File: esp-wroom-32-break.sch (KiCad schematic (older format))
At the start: 17 parts, among them CON1 Micro_SD_Card, IC1 FT232RQ, P1 CONN_01X18, P2 CONN_01X18, P3 USB_OTG, P4 Switch, U1 ESP32-WROOM, U2 NJU7223DL1-33

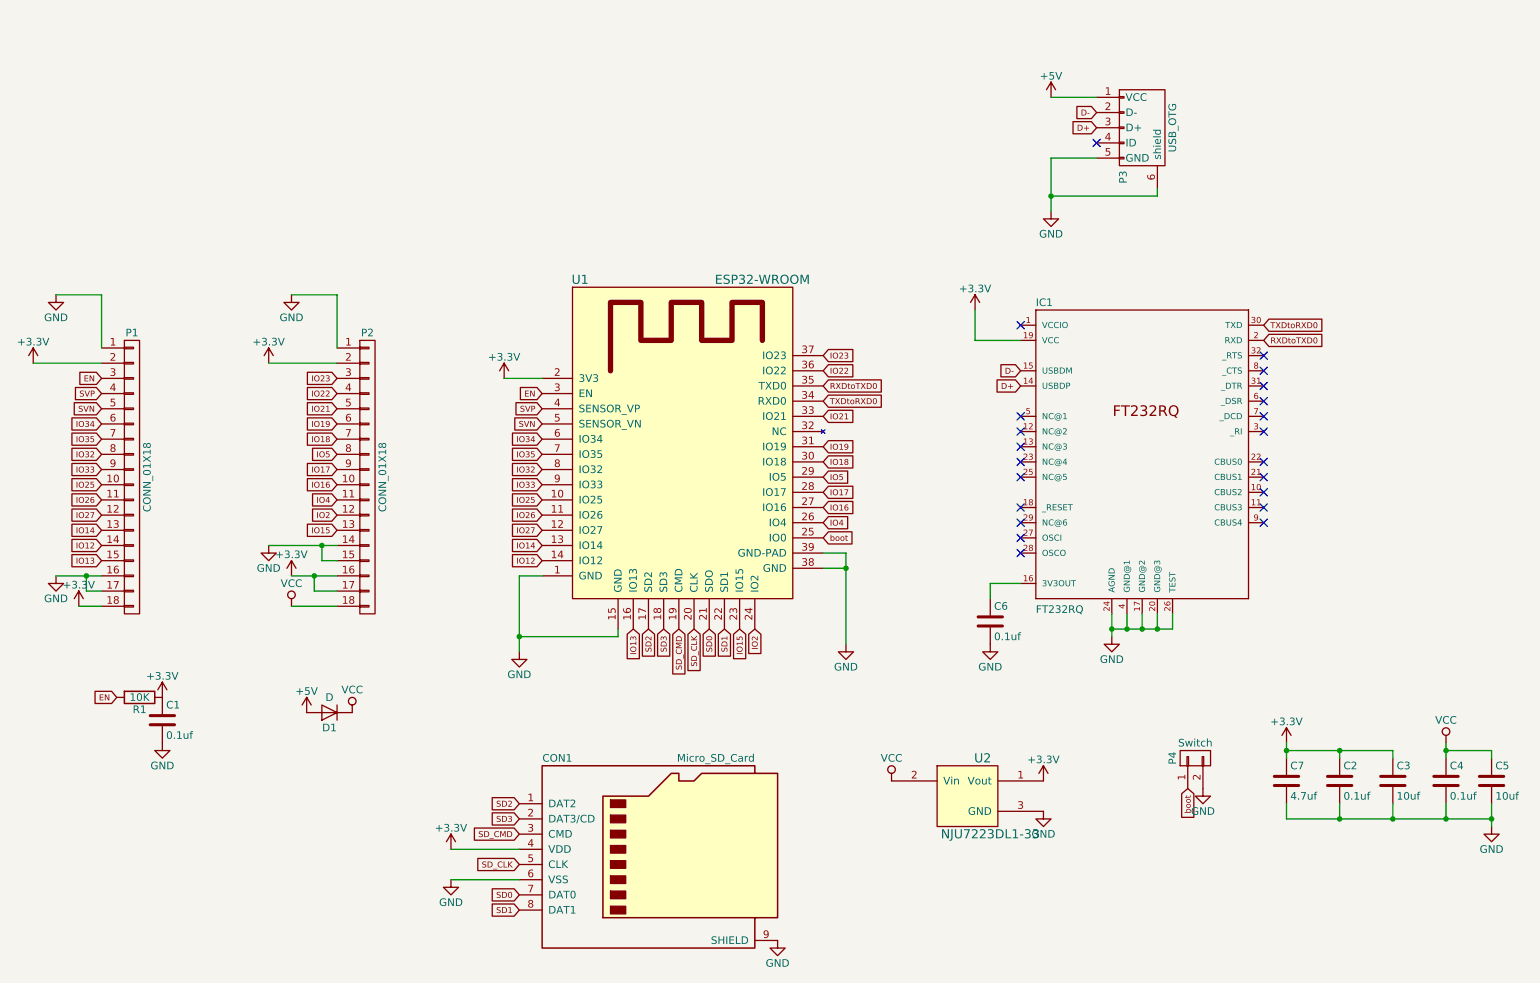
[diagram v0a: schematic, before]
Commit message: Change to 17 pins socket and remove redundant condensors
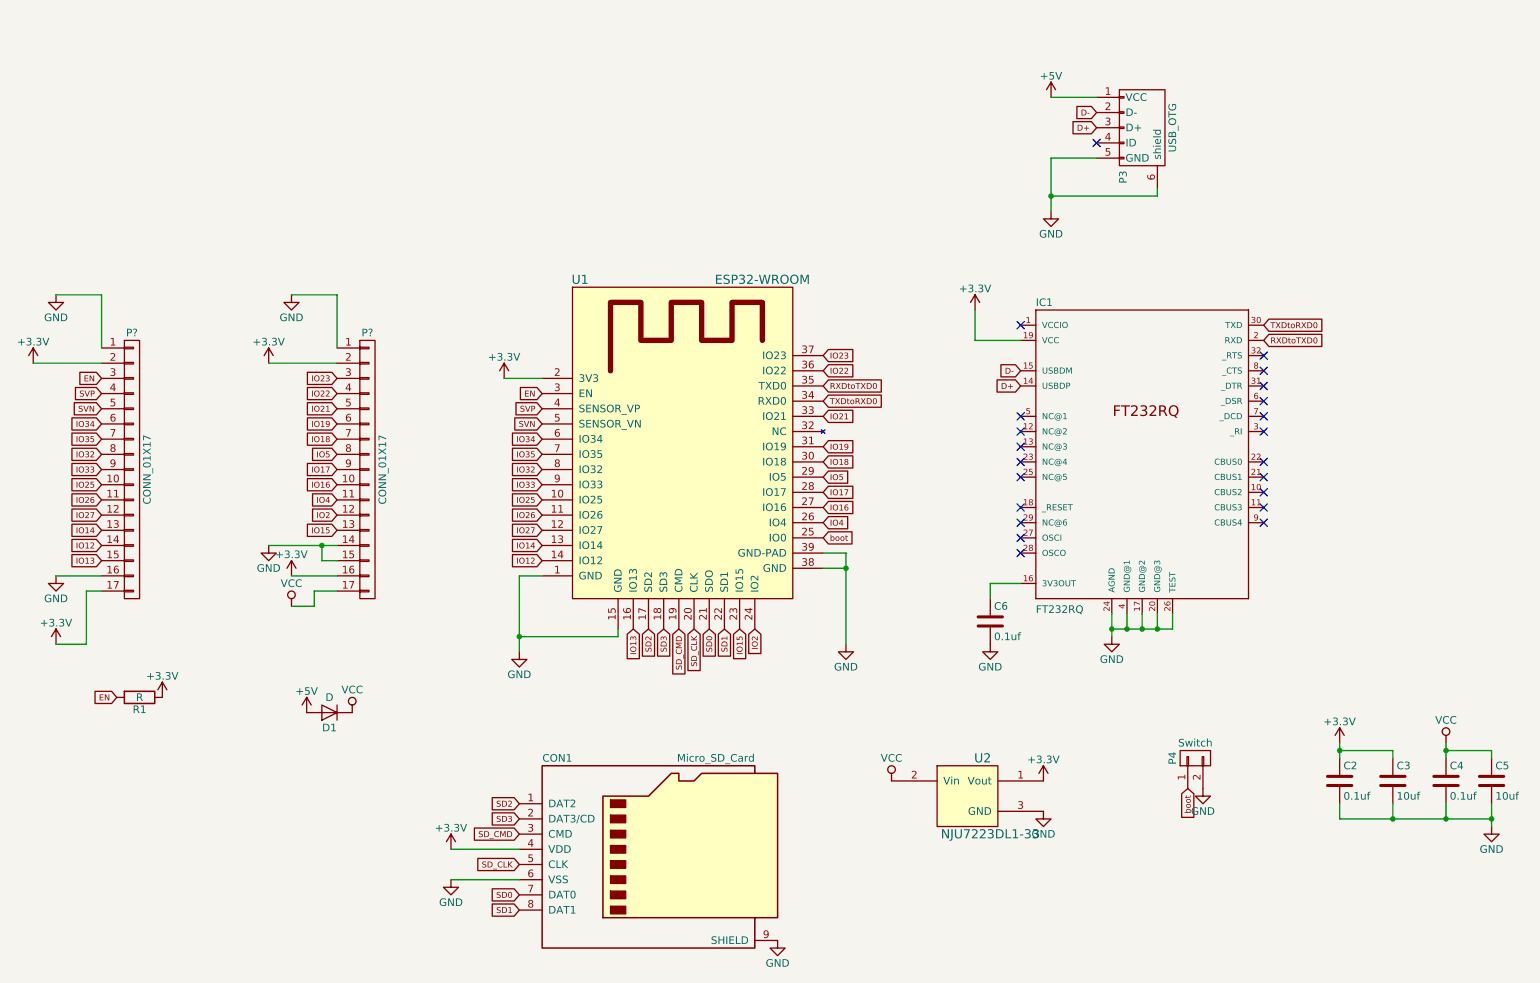
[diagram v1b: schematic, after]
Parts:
- removed C1: 0.1uf, Capacitors_SMD:C_0603, symbol C
- removed C7: 4.7uf, Capacitors_SMD:C_0603, symbol C
- removed P1, P2: CONN_01X18, Pin_Headers:Pin_Header_Straight_1x18_Pitch2.54mm, symbol CONN_01X18
- added P? (x2): CONN_01X17, symbol CONN_01X17
- R1: value 10K -> R
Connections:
- net +3V3: now also P?.16 (P16), P?.17 (P17), P?.2 (P2), P?.2 (P2)
- net EN: now also P?.3 (P3)
- net GND: now also P?.1 (P1), P?.1 (P1), P?.14 (P14), P?.15 (P15), P?.16 (P16)
- net IO12: now also P?.14 (P14)
- net IO13: now also P?.15 (P15)
- net IO14: now also P?.13 (P13)
- net IO15: now also P?.13 (P13)
- net IO16: now also P?.10 (P10)
- net IO17: now also P?.9 (P9)
- net IO18: now also P?.7 (P7)
- net IO19: now also P?.6 (P6)
- net IO2: now also P?.12 (P12)
- net IO21: now also P?.5 (P5)
- net IO22: now also P?.4 (P4)
- net IO23: now also P?.3 (P3)
- net IO25: now also P?.10 (P10)
- net IO26: now also P?.11 (P11)
- net IO27: now also P?.12 (P12)
- net IO32: now also P?.8 (P8)
- net IO33: now also P?.9 (P9)
- net IO34: now also P?.6 (P6)
- net IO35: now also P?.7 (P7)
- net IO4: now also P?.11 (P11)
- net IO5: now also P?.8 (P8)
- net SVN: now also P?.5 (P5)
- net SVP: now also P?.4 (P4)
- net VCC: now also P?.17 (P17)
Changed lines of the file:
@@
 IO15
-$Comp
-L CONN_01X18 P1
-U 1 1 5894820C
-P 1850 3800
-F 0 "P1" H 1850 4750 50  0000 C CNN
-F 1 "CONN_01X18" V 1950 3800 50  0000 C CNN
-F 2 "Pin_Headers:Pin_Header_Straight_1x18_Pitch2.54mm" H 1850 3800 50  0001 C CNN
-F 3 "" H 1850 3800 50  0000 C CNN
-	1    1850 3800
-	1    0    0    -1
-$EndComp
-$Comp
-L CONN_01X18 P2
-U 1 1 5894825B
-P 3400 3800
-F 0 "P2" H 3400 4750 50  0000 C CNN
-F 1 "CONN_01X18" V 3500 3800 50  0000 C CNN
-F 2 "Pin_Headers:Pin_Header_Straight_1x18_Pitch2.54mm" H 3400 3800 50  0001 C CNN
-F 3 "" H 3400 3800 50  0000 C CNN
-	1    3400 3800
-	1    0    0    -1
-$EndComp
 $Comp
 L +3.3V #PWR011
@@
 L +3.3V #PWR017
 U 1 1 58948E57
-P 1500 4650
-F 0 "#PWR017" H 1500 4500 50  0001 C CNN
-F 1 "+3.3V" H 1500 4790 50  0000 C CNN
-F 2 "" H 1500 4650 50  0000 C CNN
-F 3 "" H 1500 4650 50  0000 C CNN
-	1    1500 4650
+P 1350 4900
+F 0 "#PWR017" H 1350 4750 50  0001 C CNN
+F 1 "+3.3V" H 1350 5040 50  0000 C CNN
+F 2 "" H 1350 4900 50  0000 C CNN
+F 3 "" H 1350 4900 50  0000 C CNN
+	1    1350 4900
 	1    0    0    -1
 $EndComp
@@
 P 1900 5250
 F 0 "R1" V 1980 5250 50  0000 C CNN
-F 1 "10K" V 1900 5250 50  0000 C CNN
+F 1 "R" V 1900 5250 50  0000 C CNN
 F 2 "Resistors_SMD:R_0603" V 1830 5250 50  0001 C CNN
 F 3 "" H 1900 5250 50  0000 C CNN
@@
 F 3 "" H 2050 5250 50  0000 C CNN
 	1    2050 5250
-	1    0    0    -1
-$EndComp
-$Comp
-L C C1
-U 1 1 589493A7
-P 2050 5400
-F 0 "C1" H 2075 5500 50  0000 L CNN
-F 1 "0.1uf" H 2075 5300 50  0000 L CNN
-F 2 "Capacitors_SMD:C_0603" H 2088 5250 50  0001 C CNN
-F 3 "" H 2050 5400 50  0000 C CNN
-	1    2050 5400
-	1    0    0    -1
-$EndComp
-$Comp
-L GND #PWR021
-U 1 1 589493DB
-P 2050 5550
-F 0 "#PWR021" H 2050 5300 50  0001 C CNN
-F 1 "GND" H 2050 5400 50  0000 C CNN
-F 2 "" H 2050 5550 50  0000 C CNN
-F 3 "" H 2050 5550 50  0000 C CNN
-	1    2050 5550
 	1    0    0    -1
 $EndComp
@@
 L +3.3V #PWR026
 U 1 1 5894AD31
-P 9450 5550
-F 0 "#PWR026" H 9450 5400 50  0001 C CNN
-F 1 "+3.3V" H 9450 5690 50  0000 C CNN
-F 2 "" H 9450 5550 50  0000 C CNN
-F 3 "" H 9450 5550 50  0000 C CNN
-	1    9450 5550
+P 9800 5550
+F 0 "#PWR026" H 9800 5400 50  0001 C CNN
+F 1 "+3.3V" H 9800 5690 50  0000 C CNN
+F 2 "" H 9800 5550 50  0000 C CNN
+F 3 "" H 9800 5550 50  0000 C CNN
+	1    9800 5550
 	1    0    0    -1
 $EndComp
@@
 	1    0    0    -1
 $EndComp
-Wire Wire Line
-	4300 3150 4550 3150
-Wire Wire Line
-	6400 4300 6550 4300
-Wire Wire Line
-	6550 4300 6550 4900
-Wire Wire Line
-	6400 4400 6550 4400
-Connection ~ 6550 4400
-Wire Wire Line
-	4550 4450 4400 4450
-Wire Wire Line
-	4400 4450 4400 4950
-Wire Wire Line
-	5050 4800 5050 4850
-Wire Wire Line
-	5050 4850 4400 4850
-Connection ~ 4400 4850
-Wire Wire Line
-	7900 1300 8200 1300
-Wire Wire Line
-	7900 1700 8200 1700
-Wire Wire Line
-	3950 6250 4400 6250
-Wire Wire Line
-	3950 6450 4400 6450
-Wire Wire Line
-	1650 3050 1200 3050
-Wire Wire Line
-	1350 2600 1650 2600
-Wire Wire Line
-	1650 2600 1650 2950
-Wire Wire Line
-	3200 3050 2750 3050
-Wire Wire Line
-	2900 2600 3200 2600
-Wire Wire Line
-	3200 2600 3200 2950
-Wire Wire Line
-	2900 4650 3200 4650
-Wire Wire Line
-	2900 4450 3200 4450
-Wire Wire Line
-	3050 4450 3050 4550
-Wire Wire Line
-	3050 4550 3200 4550
-Connection ~ 3050 4450
-Wire Wire Line
-	1500 4650 1650 4650
-Wire Wire Line
-	1350 4450 1650 4450
-Wire Wire Line
-	1550 4450 1550 4550
-Wire Wire Line
-	1550 4550 1650 4550
-Connection ~ 1550 4450
-Wire Wire Line
-	2750 4250 3200 4250
-Wire Wire Line
-	3100 4250 3100 4350
-Wire Wire Line
-	3100 4350 3200 4350
-Connection ~ 3100 4250
-Wire Wire Line
-	7400 2900 7700 2900
-Wire Wire Line
-	8300 4700 8300 4850
-Wire Wire Line
-	8300 4800 8700 4800
-Wire Wire Line
-	8700 4800 8700 4700
-Connection ~ 8300 4800
-Wire Wire Line
-	8400 4700 8400 4800
-Connection ~ 8400 4800
-Wire Wire Line
-	8500 4700 8500 4800
-Connection ~ 8500 4800
-Wire Wire Line
-	8600 4700 8600 4800
-Connection ~ 8600 4800
-Wire Wire Line
-	7400 2700 7400 2900
-Wire Wire Line
-	10150 5600 10150 5650
-Wire Wire Line
-	10500 5550 10500 5650
-Wire Wire Line
-	10500 5600 10800 5600
-Wire Wire Line
-	10800 5600 10800 5650
-Connection ~ 10500 5600
-Wire Wire Line
-	9800 5950 9800 6050
-Wire Wire Line
-	9450 6050 10800 6050
-Wire Wire Line
-	10800 5950 10800 6100
-Connection ~ 10800 6050
-Wire Wire Line
-	10500 5950 10500 6050
-Connection ~ 10500 6050
-Wire Wire Line
-	10150 5950 10150 6050
-Connection ~ 10150 6050
 $Comp
 L NJU7223DL1-33 U2
@@
 $EndComp
 NoConn ~ 7700 2800
-Wire Wire Line
-	7900 1700 7900 2050
-Wire Wire Line
-	8600 1900 8600 1950
-Wire Wire Line
-	8600 1950 7900 1950
-Connection ~ 7900 1950
 $Comp
 L FT232RQ IC1
@@
 	1    0    0    -1
 $EndComp
+$Comp
+L CONN_01X17 P?
+U 1 1 58A7A438
+P 1850 3750
+F 0 "P?" H 1850 4650 50  0000 C CNN
+F 1 "CONN_01X17" V 1950 3750 50  0000 C CNN
+F 2 "" H 1850 3750 50  0000 C CNN
+F 3 "" H 1850 3750 50  0000 C CNN
+	1    1850 3750
+	1    0    0    -1
+$EndComp
+$Comp
+L CONN_01X17 P?
+U 1 1 58A7A491
+P 3400 3750
+F 0 "P?" H 3400 4650 50  0000 C CNN
+F 1 "CONN_01X17" V 3500 3750 50  0000 C CNN
+F 2 "" H 3400 3750 50  0000 C CNN
+F 3 "" H 3400 3750 50  0000 C CNN
+	1    3400 3750
+	1    0    0    -1
+$EndComp
+Wire Wire Line
+	4300 3150 4550 3150
+Wire Wire Line
+	6400 4300 6550 4300
+Wire Wire Line
+	6550 4300 6550 4900
+Wire Wire Line
+	6400 4400 6550 4400
+Connection ~ 6550 4400
+Wire Wire Line
+	4550 4450 4400 4450
+Wire Wire Line
+	4400 4450 4400 4950
+Wire Wire Line
+	5050 4800 5050 4850
+Wire Wire Line
+	5050 4850 4400 4850
+Connection ~ 4400 4850
+Wire Wire Line
+	7900 1300 8200 1300
+Wire Wire Line
+	7900 1700 8200 1700
+Wire Wire Line
+	3950 6250 4400 6250
+Wire Wire Line
+	3950 6450 4400 6450
+Wire Wire Line
+	1650 3050 1200 3050
+Wire Wire Line
+	1350 2600 1650 2600
+Wire Wire Line
+	1650 2600 1650 2950
+Wire Wire Line
+	3200 3050 2750 3050
+Wire Wire Line
+	2900 2600 3200 2600
+Wire Wire Line
+	3200 2600 3200 2950
+Wire Wire Line
+	2900 4450 3200 4450
+Wire Wire Line
+	1350 4450 1650 4450
+Wire Wire Line
+	2750 4250 3200 4250
+Wire Wire Line
+	3100 4250 3100 4350
+Wire Wire Line
+	3100 4350 3200 4350
+Connection ~ 3100 4250
+Wire Wire Line
+	7400 2900 7700 2900
+Wire Wire Line
+	8300 4700 8300 4850
+Wire Wire Line
+	8300 4800 8700 4800
+Wire Wire Line
+	8700 4800 8700 4700
+Connection ~ 8300 4800
+Wire Wire Line
+	8400 4700 8400 4800
+Connection ~ 8400 4800
+Wire Wire Line
+	8500 4700 8500 4800
+Connection ~ 8500 4800
+Wire Wire Line
+	8600 4700 8600 4800
+Connection ~ 8600 4800
+Wire Wire Line
+	7400 2700 7400 2900
+Wire Wire Line
+	10150 5600 10150 5650
+Wire Wire Line
+	10500 5550 10500 5650
+Wire Wire Line
+	10500 5600 10800 5600
+Wire Wire Line
+	10800 5600 10800 5650
+Connection ~ 10500 5600
+Wire Wire Line
+	10800 5950 10800 6100
+Connection ~ 10800 6050
+Wire Wire Line
+	10500 5950 10500 6050
+Connection ~ 10500 6050
+Wire Wire Line
+	10150 5950 10150 6050
+Connection ~ 10150 6050
+Wire Wire Line
+	7900 1700 7900 2050
+Wire Wire Line
+	8600 1900 8600 1950
+Wire Wire Line
+	8600 1950 7900 1950
+Connection ~ 7900 1950
 Wire Wire Line
 	7500 4600 7500 4500
 Wire Wire Line
 	7500 4500 7700 4500
-$Comp
-L C C7
-U 1 1 58987CEA
-P 9450 5800
-F 0 "C7" H 9475 5900 50  0000 L CNN
-F 1 "4.7uf" H 9475 5700 50  0000 L CNN
-F 2 "Capacitors_SMD:C_0603" H 9488 5650 50  0001 C CNN
-F 3 "" H 9450 5800 50  0000 C CNN
-	1    9450 5800
-	1    0    0    -1
-$EndComp
-Wire Wire Line
-	9450 5550 9450 5650
-Wire Wire Line
-	9450 5950 9450 6050
-Connection ~ 9800 6050
-Wire Wire Line
-	10150 5600 9450 5600
-Connection ~ 9450 5600
-Wire Wire Line
-	9800 5650 9800 5600
+Wire Wire Line
+	1650 4550 1550 4550
+Wire Wire Line
+	1550 4550 1550 4900
+Wire Wire Line
+	1550 4900 1350 4900
+Wire Wire Line
+	2900 4650 3050 4650
+Wire Wire Line
+	3050 4650 3050 4550
+Wire Wire Line
+	3050 4550 3200 4550
+Wire Wire Line
+	9800 5550 9800 5650
+Wire Wire Line
+	9800 5600 10150 5600
 Connection ~ 9800 5600
+Wire Wire Line
+	9800 5950 9800 6050
+Wire Wire Line
+	9800 6050 10800 6050
 $EndSCHEMATC

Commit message: Update schema and netlist with adding auto reset circuit
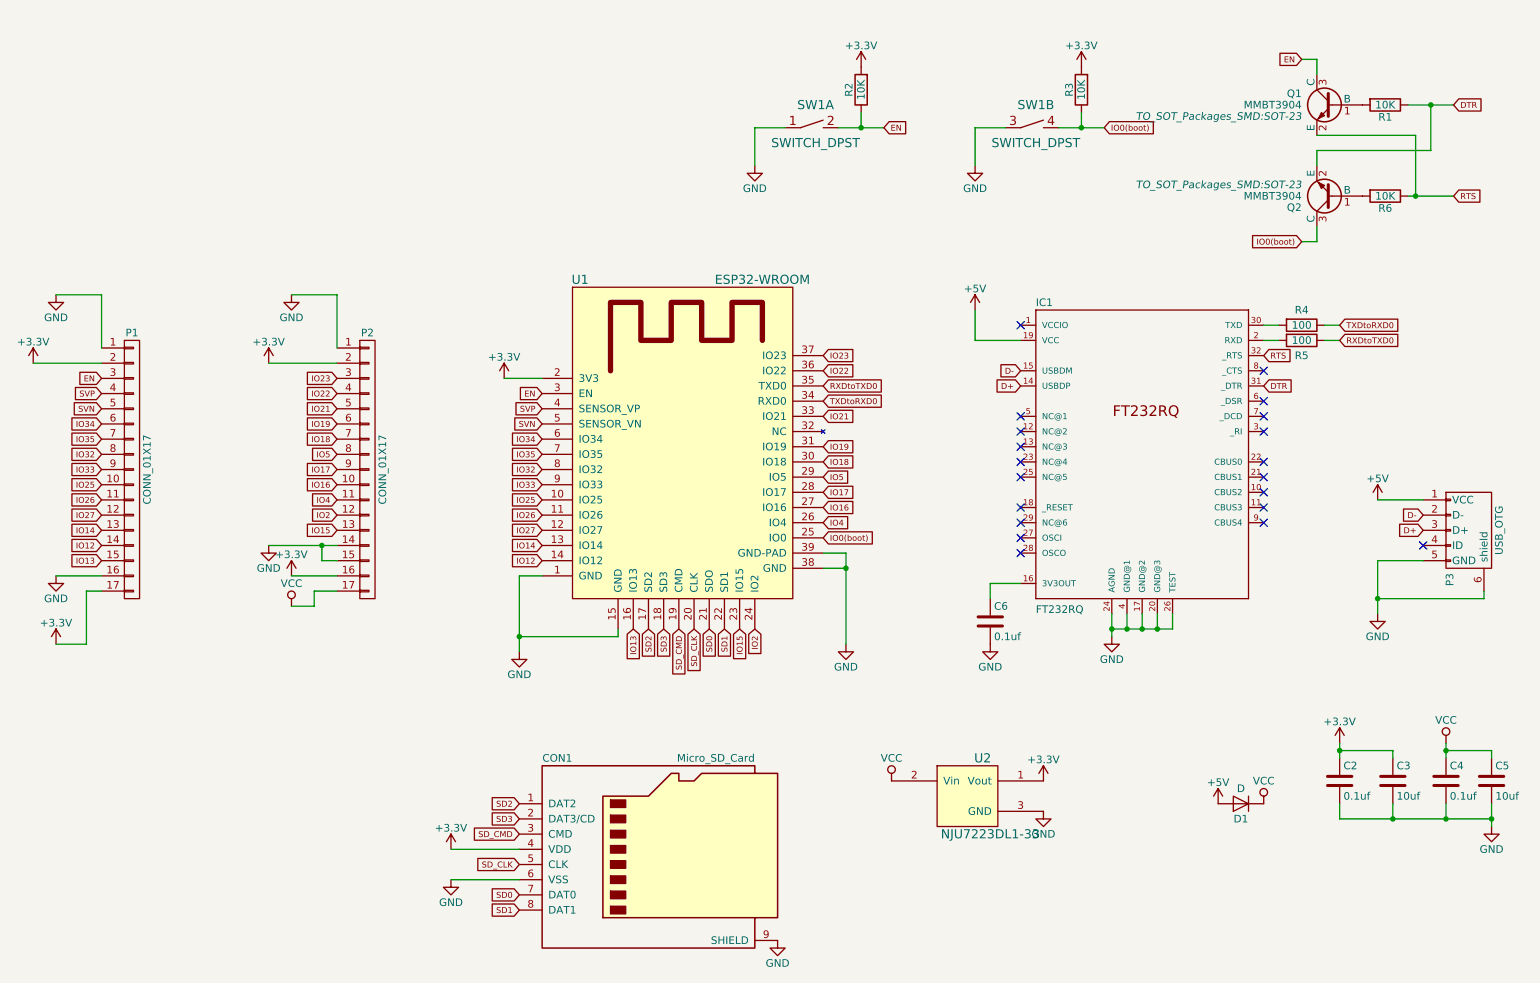
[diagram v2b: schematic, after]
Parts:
- removed P4: Switch, Buttons_Switches_SMD:SW_SPST_B3S-1000, symbol CONN_01X02
- added Q1, Q2: MMBT3904, TO_SOT_Packages_SMD:SOT-23, symbol MMBT3904
- added R2, R3, R6: 10K, Resistors_SMD:R_0603, symbol R
- added R4, R5: 100, Resistors_SMD:R_0603, symbol R
- added SW1: SWITCH_DPST, symbol SWITCH_DPST
- P1, P2: renamed from P?; footprint (none) -> Pin_Headers:Pin_Header_Straight_1x17_Pitch2.00mm
- R1: value R -> 10K
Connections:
- net +3V3: now also R2.2, R3.2; no longer IC1.19 (VCC), R1.1
- net +5V: now also IC1.19 (VCC)
- net EN: now also Q1.3 (C), R2.1, SW1.2; no longer R1.2
- net GND: now also SW1.1, SW1.3
- net RXDtoTXD0: now also R5.1; no longer IC1.2 (RXD)
- net TXDtoRXD0: now also R4.1; no longer IC1.30 (TXD)
- net DTR: now reaches IC1.31 (_DTR)
- net DTR: now also R1.1, Q2.2 (E)
- net RTS: now reaches IC1.32 (_RTS)
- net RTS: now also Q1.2 (E), R6.1
- net boot renamed IO0(boot)
- net IO0(boot): now also Q2.3 (C), R3.1, SW1.4
- new net: Q1.1 (B), R1.2
- new net: IC1.2 (RXD), R5.2
- new net: IC1.30 (TXD), R4.2
- new net: Q2.1 (B), R6.2
- no-connect marks 22 -> 20
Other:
- moved on the sheet: D1, P3, R1
